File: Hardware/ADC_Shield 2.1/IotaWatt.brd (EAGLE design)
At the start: 53.6 x 61 mm, 58 parts, among them J0 STEREO_JACK_BOT, J1 STEREO_JACK_BOT, J2 STEREO_JACK_BOT, J3 STEREO_JACK_BOT, J4 STEREO_JACK_BOT, J5 STEREO_JACK_BOT, J6 STEREO_JACK_BOT

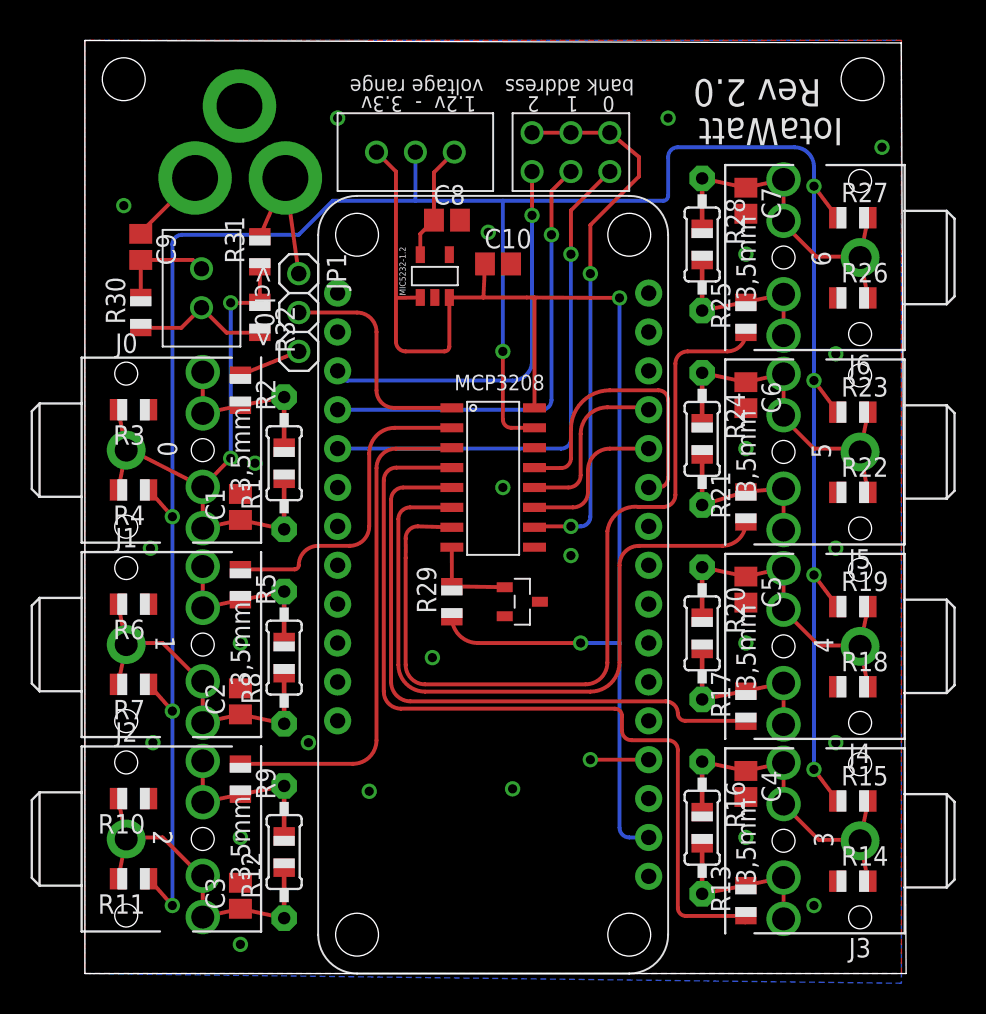
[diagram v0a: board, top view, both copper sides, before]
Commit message: Add index to logfile and other significant changes.
Adds an index file to the SD that identifies gaps in the regular
intervals of entries.  A second level index is created in memory to
further increase API performance.  Added VT phase calibration aids.
Other improvements to config/status app.
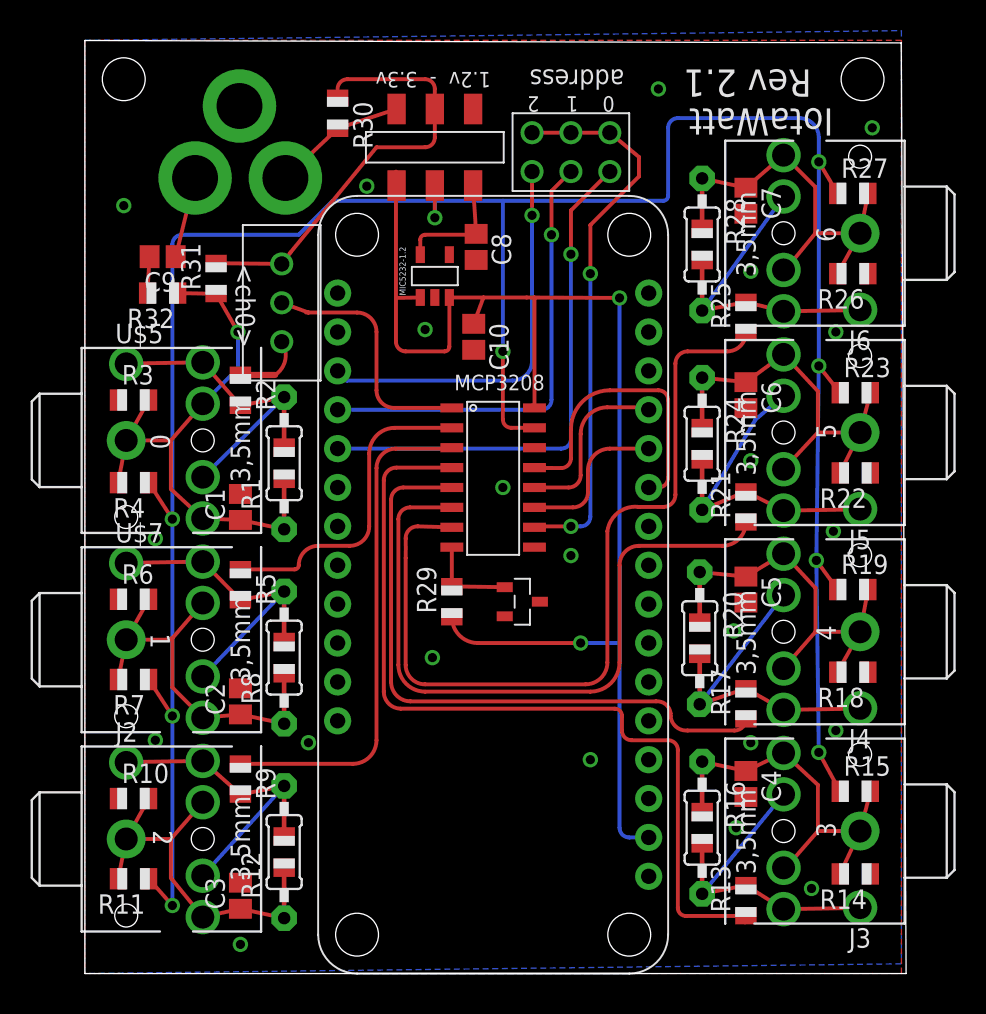
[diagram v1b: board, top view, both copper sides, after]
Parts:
- removed J0, J1: STEREO_JACK_BOT, IotaWatt_parts:STX3100
- removed JP1: (no value), adafruit:1X03
- removed JP2: HEADER_1X2, IotaWatt_parts:HEADER_1X2
- removed U$2: HEADER_1X3, IotaWatt_parts:HEADER_1X3
- added U$5, U$7: STEREO_JACK_BOT, IotaWatt_parts:STX3100
- added U$6: HEADER_1X3, IotaWatt_parts:HEADER_1X3
- added U$8: DPDT_SMT_SW, IotaWatt_parts:JS202011SCQN
- moved R30 18.3 mm to (16.5, 56.2), turned to 270 degrees
- moved R32 6.55 mm to (5.08, 44.5), turned to 180 degrees
- moved C10 5.02 mm to (25.4, 41.6), turned to 270 degrees
- moved R31 3.35 mm to (8.57, 45.4)
- moved C8 2.58 mm to (25.6, 47.5), turned to 270 degrees
- moved J6 1.59 mm to (53.3, 48.3)
- moved R26 1.59 mm to (50.2, 45.7), turned to 180 degrees
- moved R27 1.59 mm to (50.2, 51.0)
- moved C9 1.56 mm to (5.08, 46.8), turned to 180 degrees
- moved R22 1.28 mm to (50.3, 32.7), turned to 180 degrees
- moved R23 1.28 mm to (50.3, 37.9)
- moved J5 1.27 mm to (53.3, 35.2)
- moved R19 1.11 mm to (50.2, 25.1)
- moved J4 0.95 mm to (53.3, 22.2)
- moved R18 0.95 mm to (50.2, 19.7), turned to 180 degrees
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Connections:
- removed net ACV1: C9.2, JP2.2, R30.2
- removed net ACV2: JP2.1, R30.1, R32.2
- removed net N$8: JP1.1, R31.2, U$3.TIP
- new net N$11: R1.2, R2.2, U$5.2, U$5.4
- new net SW1-4: R30.2, U$3.TIP, U$8.P$4
- new net SW1-5: R30.1, R31.2, U$6.1, U$8.P$5
- net 3V3: now also U$8.P$1; no longer U$2.1
- net ADC0: now also U$6.2; no longer JP1.2
- net AREF: now also U$8.P$2; no longer U$2.2
- net N$1: now also U$6.3; no longer JP1.3
- net N$12: now also J2.3; no longer J2.4
- net N$13: now also J4.3; no longer J4.4
- net N$14: now also J5.4; no longer J5.3
- net N$16: now also J5.3; no longer J5.4
- net N$17: now also C9.2, R32.2; no longer J0.2, J0.3, R1.2, R2.2
- net N$18: now also J6.4; no longer J6.3
- net N$19: now also J6.3; no longer J6.4
- net N$2: now also U$5.1, U$5.3, U$5.5; no longer J0.1, J0.4, J0.5
- net N$20: now also U$7.2, U$7.4; no longer J1.2, J1.3
- net N$21: now also J3.4; no longer J3.3
- net N$22: now also J3.3; no longer J3.4
- net N$24: now also U$8.P$3; no longer U$2.3
- net N$26: now also J4.4; no longer J4.3
- net N$4: now also U$7.1, U$7.3, U$7.5; no longer J1.1, J1.4, J1.5
- net N$5: now also J2.4; no longer J2.3
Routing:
- net SW1-5: track 0.00 -> 28.2 mm
- net N$11: track 0.00 -> 19.1 mm
- net N$14: track 8.16 -> 20.3 mm
- net N$26: track 8.12 -> 19.9 mm
- net N$18: track 8.12 -> 19.4 mm
- net N$21: track 8.12 -> 19.4 mm
- net N$5: track 8.12 -> 19.1 mm
- net N$20: track 8.12 -> 19.1 mm
- net N$8: track 10.5 -> 0.00 mm
- net ACV2: track 9.00 -> 0.00 mm
- net SW1-4: track 0.00 -> 8.75 mm
- net ACV1: track 6.64 -> 0.00 mm
- net N$17: track 8.12 -> 2.39 mm
- net N$19: track 19.6 -> 24.1 mm
- net N$13: track 19.5 -> 23.9 mm
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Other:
- board text added: "Rev 2.1"
- board text added: "address"
- board text removed: "Rev 2.0"
- board text removed: "bank address"
- board text removed: "voltage range"
